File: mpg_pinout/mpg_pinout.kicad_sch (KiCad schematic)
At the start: 9 parts, among them J1 Conn_02x05_Odd_Even, J2 Conn_01x02_Pin, J3 Conn_01x02_Pin, J4 Conn_01x02_Pin, J5 Conn_01x02_Pin, J6 Conn_01x02_Pin, J7 Conn_01x02_Pin, J8 Conn_01x02_Pin

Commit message: third commit
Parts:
- added R2, R3, R5, R6: R, Resistor_THT:R_Axial_DIN0414_L11.9mm_D4.5mm_P15.24mm_Horizontal, symbol Device:R
- added R4: R, Resistor_THT:R_Axial_DIN0414_L11.9mm_D4.5mm_P25.40mm_Horizontal, symbol Device:R
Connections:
- net at J5.1 (Pin_1): now also R6.1; no longer J1.4 (Pin_4)
- net at J5.2 (Pin_2): now also R2.2; no longer J1.3 (Pin_3)
- net at J4.1 (Pin_1): now also R4.1; no longer J1.5 (Pin_5)
- net at J4.2 (Pin_2): now also R5.1; no longer J1.6 (Pin_6)
- net at J1.7 (Pin_7): now also R3.1; no longer J6.2 (Pin_2)
- new net: J6.2 (Pin_2), R3.2
- new net: J1.3 (Pin_3), R2.1
- new net: J1.4 (Pin_4), R6.2
- new net: J1.5 (Pin_5), R4.2
- new net: J1.6 (Pin_6), R5.2
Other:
- note added: "ALL RESISTORS ARE USED FOR JUMP"
- moved on the sheet: J1, R1

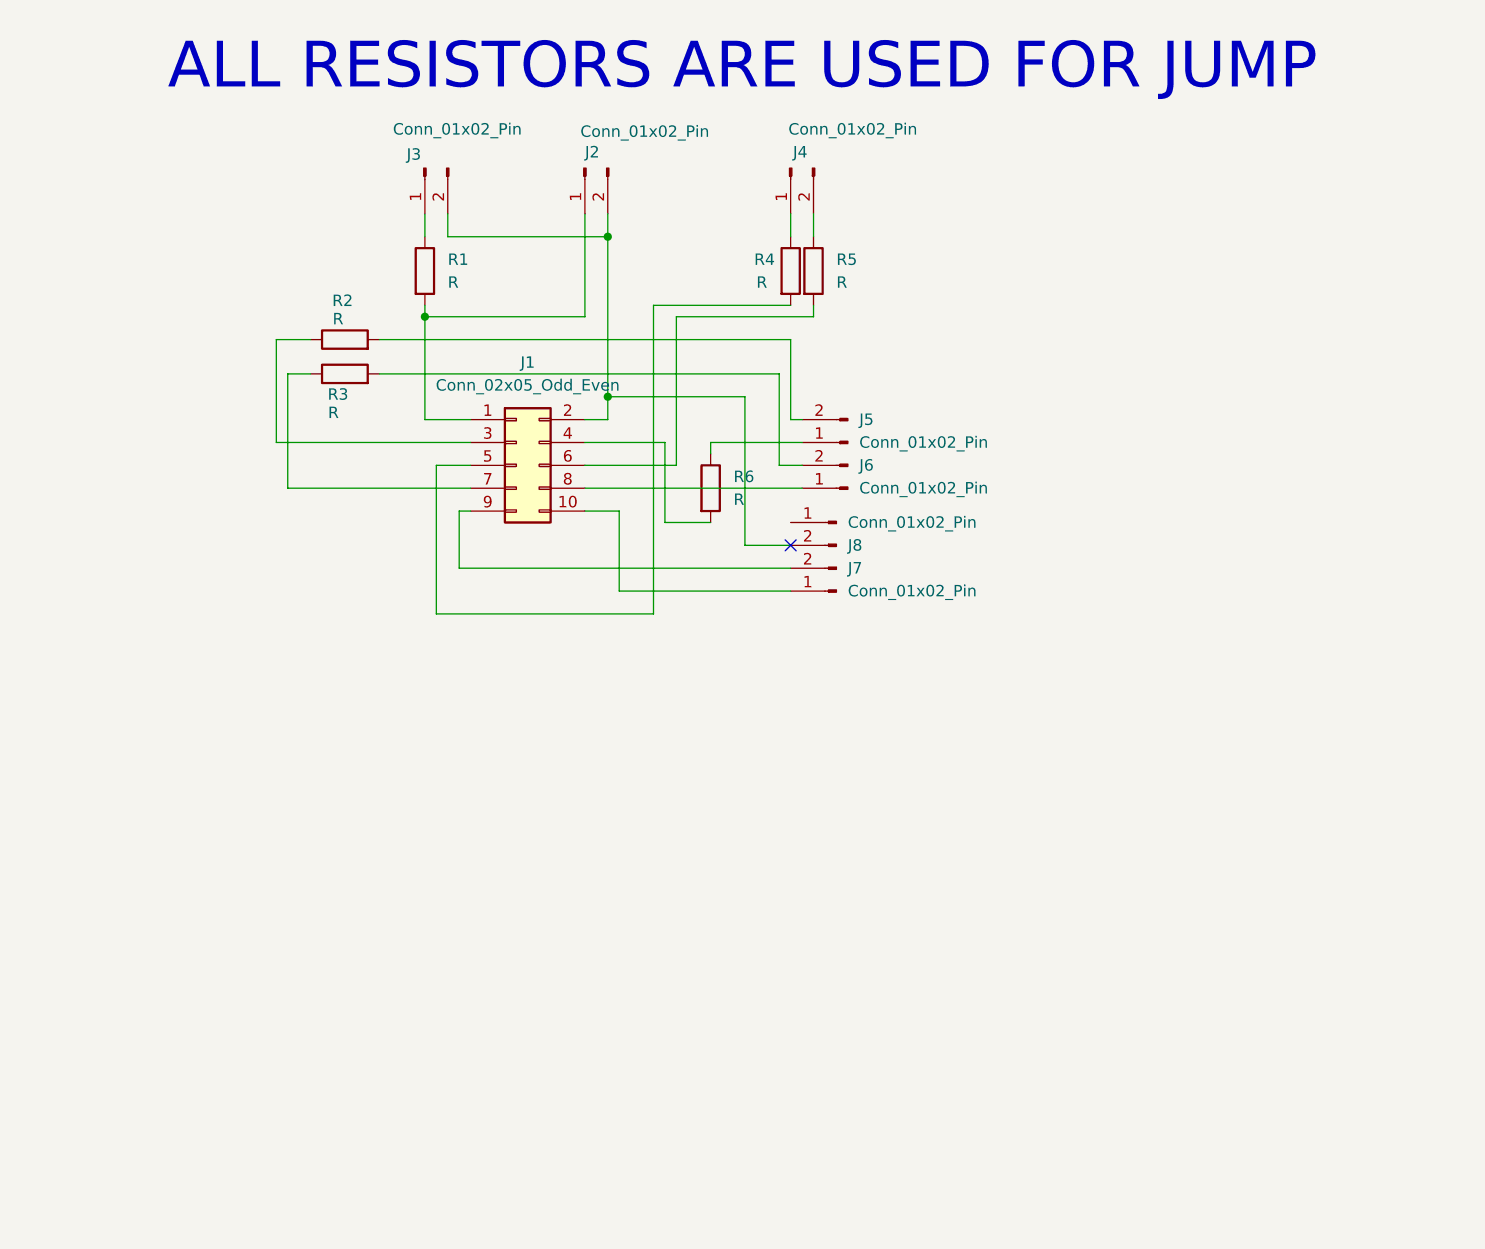
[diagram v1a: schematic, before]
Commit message: Made pdf file for mpg and bidirectional, 7x10cm
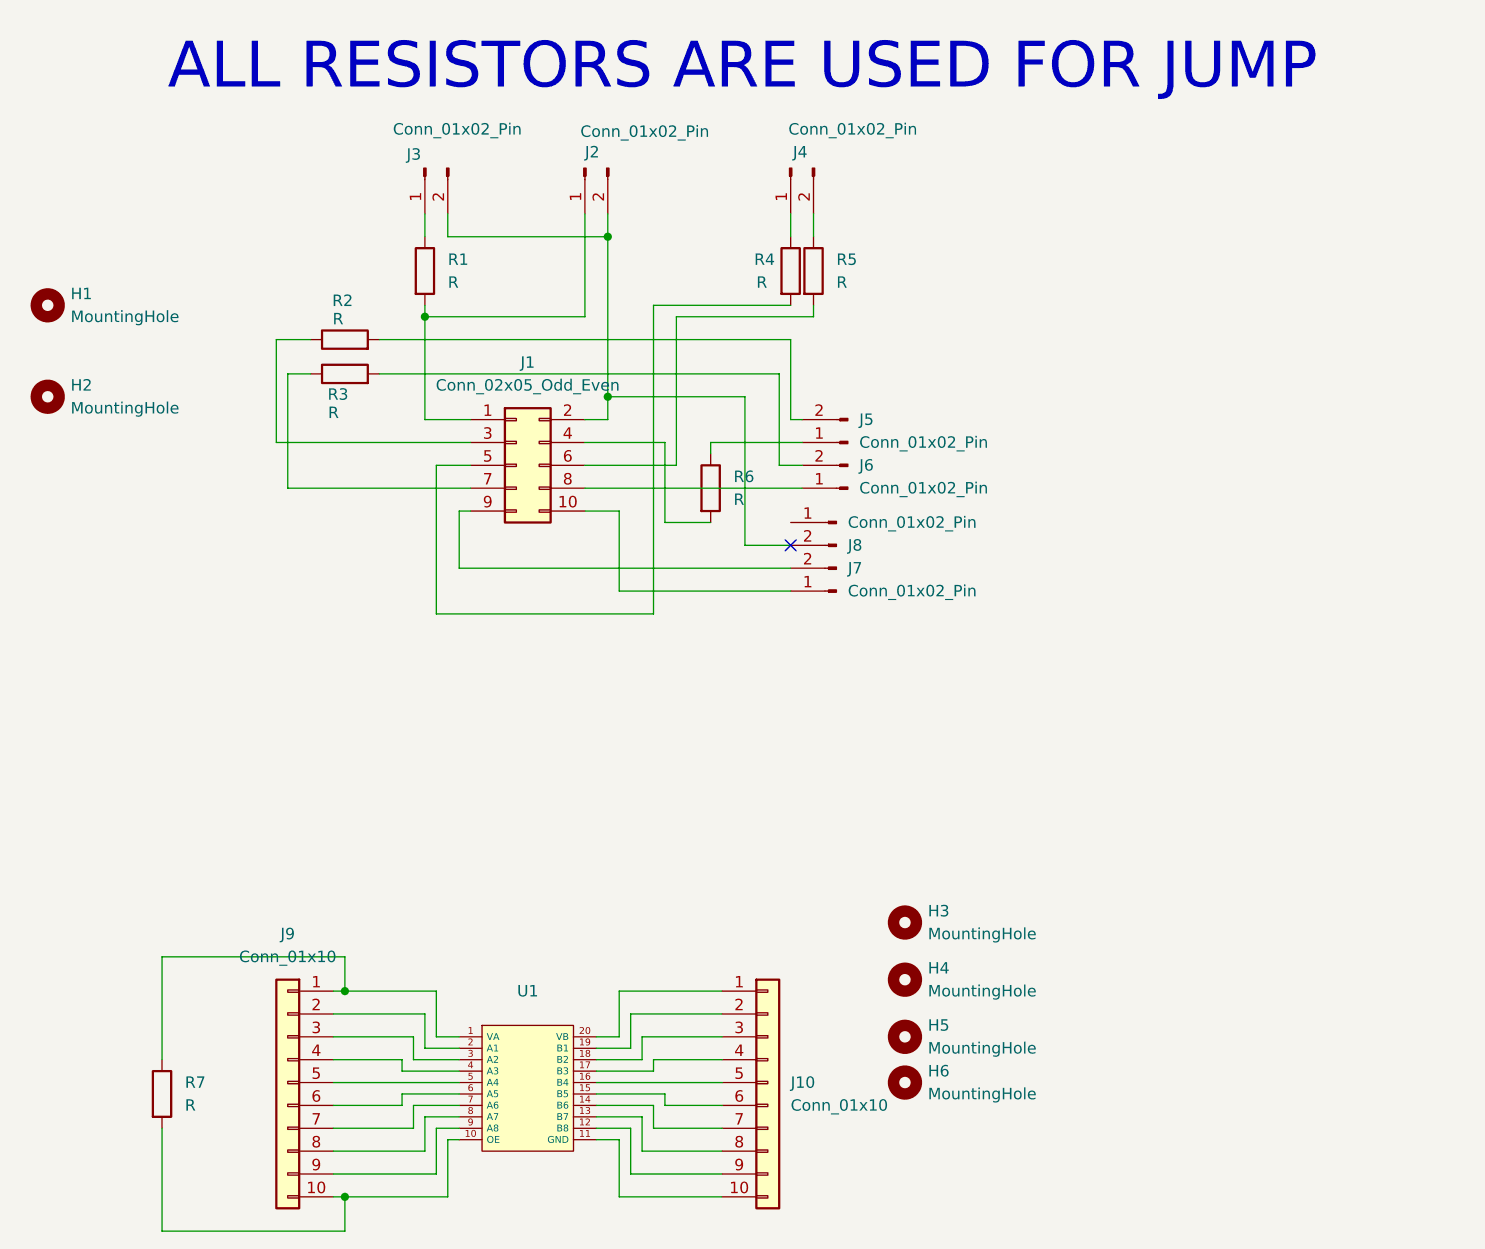
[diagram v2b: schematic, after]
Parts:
- added H1, H2, H3, H4, H5, H6: MountingHole, _customized:hole_3mm, symbol Mechanical:MountingHole
- added J10, J9: Conn_01x10, _customized:connector_01x10_508, symbol Connector_Generic:Conn_01x10
- added R7: R, Resistor_THT:R_Axial_DIN0411_L9.9mm_D3.6mm_P25.40mm_Horizontal, symbol Device:R
- added U1: ~, _customized:TXS0108, symbol _customized_symbol:TXS0108
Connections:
- new net: J9.1 (Pin_1), R7.1, U1.1 (VA)
- new net: J9.10 (Pin_10), R7.2, U1.10 (OE)
- new net: J9.2 (Pin_2), U1.2 (A1)
- new net: J9.3 (Pin_3), U1.3 (A2)
- new net: J9.4 (Pin_4), U1.4 (A3)
- new net: J9.5 (Pin_5), U1.5 (A4)
- new net: J9.6 (Pin_6), U1.6 (A5)
- new net: J9.7 (Pin_7), U1.7 (A6)
- new net: J9.8 (Pin_8), U1.8 (A7)
- new net: J9.9 (Pin_9), U1.9 (A8)
- new net: J10.10 (Pin_10), U1.11 (GND)
- new net: J10.9 (Pin_9), U1.12 (B8)
- new net: J10.8 (Pin_8), U1.13 (B7)
- new net: J10.7 (Pin_7), U1.14 (B6)
- new net: J10.6 (Pin_6), U1.15 (B5)
- new net: J10.5 (Pin_5), U1.16 (B4)
- new net: J10.4 (Pin_4), U1.17 (B3)
- new net: J10.3 (Pin_3), U1.18 (B2)
- new net: J10.2 (Pin_2), U1.19 (B1)
- new net: J10.1 (Pin_1), U1.20 (VB)
